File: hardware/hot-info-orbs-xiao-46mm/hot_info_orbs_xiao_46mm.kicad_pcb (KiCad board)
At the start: 2 copper layers, 224 x 52.8 mm, 13 parts, among them SW1 SW_Push, SW2 SW_Push, SW3 SW_Push, U2 XIAO ESP32-S3 Plus

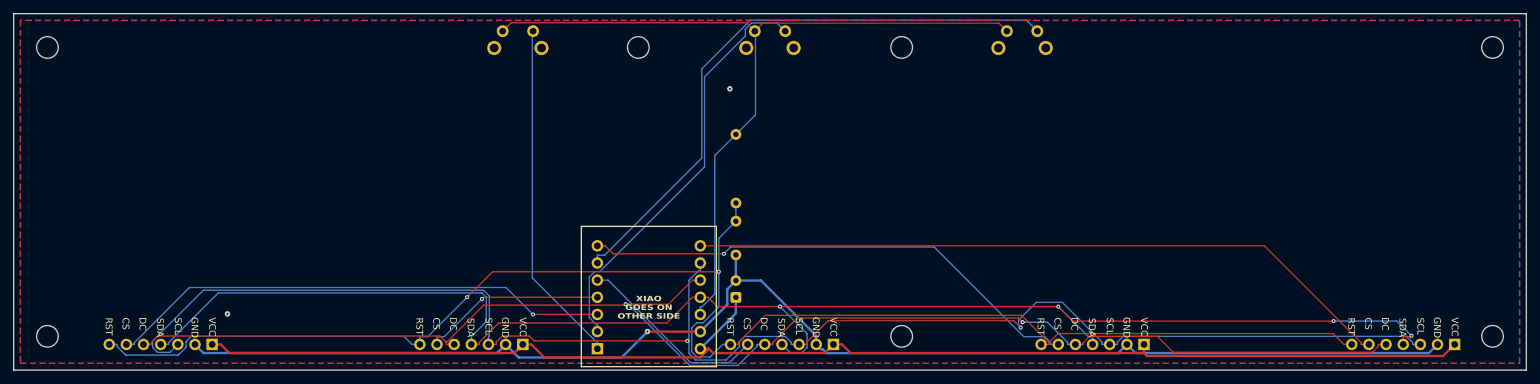
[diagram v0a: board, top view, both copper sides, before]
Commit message: board rev 2.4: Display circle on the front silk at each module position
Scott: "add circles indicating the display goes on that side, in the middle
put Display" and "increment the version". tools/display_marks.py puts a
O29.5 mm F.Silk circle with 2 mm "Display" at each DSn's 3D-model origin
(58.74 + n*46, y 81.0) and bumps rev 2.3 -> 2.4 (back silk, title block,
schematic rev). Copper, mask, outline and drill are run 3's; only the two
silk layers and the rev attribute changed.

Rejected the lit-area radius (16.25): at DS3 it crosses the front annular
rings of C1 pad 2 and XIAO pad 8, two "clipped by solder mask" DRC
warnings and two fab-cut gaps in the ring. 14.75 is the largest radius
that clears both. Rejected the module rim (19.05): past the board edge at
DS5. The DS3 circle crossing the XIAO box corner stays; silk over silk is
not a DRC item and the layout really is like that.

Package: fab/hot_info_orbs_xiao_46mm_2.4_run1_gerbers.zip; run 3 demoted
in fab/README.md. STEP regenerated and imported into overall assembly v8
(same transform, Position6), which also keeps the bezel/watch-crystal
occurrences that were sitting unsaved in the Fusion session.

Co-Authored-By: Claude Fable 5.1 <noreply@anthropic.com>
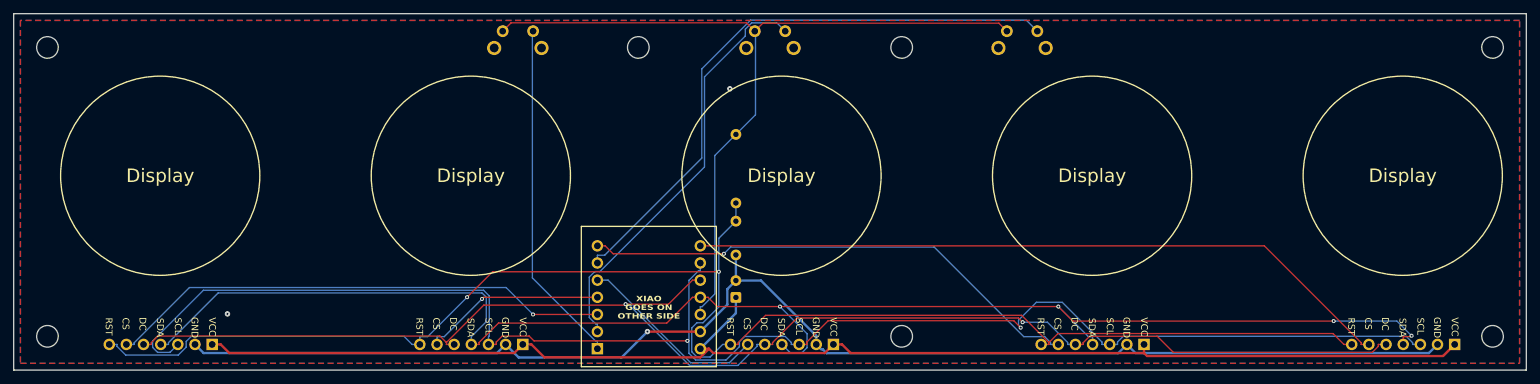
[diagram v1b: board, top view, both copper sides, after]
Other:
- board text added: "Display"
- board text added: "XIAO ESP32-S3 · rev 2.4 · 46 mm pitch"
- board text removed: "XIAO ESP32-S3 · rev 2.3 · 46 mm pitch"
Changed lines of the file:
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@@
 	(paper "A4")
 	(title_block
-		(rev "2.3")
+		(rev "2.4")
 	)
 	(layers
@@
 		)
 	)
+	(gr_circle
+		(center 58.74 81)
+		(end 73.49 81)
+		(stroke
+			(width 0.2)
+			(type default)
+		)
+		(fill no)
+		(layer "F.SilkS")
+	)
+	(gr_circle
+		(center 104.74 81)
+		(end 119.49 81)
+		(stroke
+			(width 0.2)
+			(type default)
+		)
+		(fill no)
+		(layer "F.SilkS")
+	)
 	(gr_rect
 		(start 121.1 88.5)
@@
 		(layer "F.SilkS")
 	)
+	(gr_circle
+		(center 150.739999 81)
+		(end 165.489999 81)
+		(stroke
+			(width 0.2)
+			(type default)
+		)
+		(fill no)
+		(layer "F.SilkS")
+	)
+	(gr_circle
+		(center 196.739999 81)
+		(end 211.489999 81)
+		(stroke
+			(width 0.2)
+			(type default)
+		)
+		(fill no)
+		(layer "F.SilkS")
+	)
+	(gr_circle
+		(center 242.739999 81)
+		(end 257.49 81)
+		(stroke
+			(width 0.2)
+			(type default)
+		)
+		(fill no)
+		(layer "F.SilkS")
+	)
 	(gr_line
 		(start 44.565137 83.469712)
@@
 		)
 	)
+	(gr_text "Display"
+		(at 58.74 81 0)
+		(layer "F.SilkS")
+		(effects
+			(font
+				(size 2 2)
+				(thickness 0.3)
+			)
+		)
+	)
+	(gr_text "Display"
+		(at 104.74 81 0)
+		(layer "F.SilkS")
+		(effects
+			(font
+				(size 2 2)
+				(thickness 0.3)
+			)
+		)
+	)
+	(gr_text "Display"
+		(at 150.739999 81 0)
+		(layer "F.SilkS")
+		(effects
+			(font
+				(size 2 2)
+				(thickness 0.3)
+			)
+		)
+	)
+	(gr_text "Display"
+		(at 196.739999 81 0)
+		(layer "F.SilkS")
+		(effects
+			(font
+				(size 2 2)
+				(thickness 0.3)
+			)
+		)
+	)
+	(gr_text "Display"
+		(at 242.739999 81 0)
+		(layer "F.SilkS")
+		(effects
+			(font
+				(size 2 2)
+				(thickness 0.3)
+			)
+		)
+	)
 	(gr_text "button\n"
 		(at 111.706633 64.63 0)
@@
 		)
 	)
-	(gr_text "XIAO ESP32-S3  ·  rev 2.3 · 46 mm pitch"
+	(gr_text "XIAO ESP32-S3  ·  rev 2.4 · 46 mm pitch"
 		(at 70.174 85.334052 0)
 		(layer "B.SilkS")
@@
 			(justify top mirror)
 		)
-		(render_cache "XIAO ESP32-S3  ·  rev 2.3 · 46 mm pitch" 0
+		(render_cache "XIAO ESP32-S3  ·  rev 2.4 · 46 mm pitch" 0
 			(polygon
 				(pts
@@
 			(polygon
 				(pts
-					(xy 62.649366 87.396578) (xy 62.784673 87.386522) (xy 62.907398 87.357291) (xy 63.019638 87.309505)
-					(xy 63.106201 87.252501) (xy 63.175326 87.186751) (xy 63.229006 87.111763) (xy 63.268277 87.026306)
-					(xy 63.276459 86.977945) (xy 63.266061 86.927416) (xy 63.234816 86.88611) (xy 63.189737 86.858592)
-					(xy 63.138462 86.849474) (xy 63.088583 86.861677) (xy 63.044184 86.90052) (xy 62.981292 86.995653)
-					(xy 62.924149 87.054398) (xy 62.84879 87.097136) (xy 62.760465 87.121853) (xy 62.649243 87.130841)
-					(xy 62.553323 87.120383) (xy 62.467125 87.089716) (xy 62.38827 87.038273) (xy 62.321098 86.966395)
-					(xy 62.282455 86.887521) (xy 62.269446 86.798549) (xy 62.279368 86.698783) (xy 62.307898 86.612508)
-					(xy 62.354636 86.536942) (xy 62.421121 86.470287) (xy 62.515519 86.410971) (xy 62.632332 86.3673)
-					(xy 62.776372 86.34096) (xy 62.849383 86.325314) (xy 62.894198 86.299377) (xy 62.919339 86.264663)
-					(xy 62.928047 86.218472) (xy 62.916674 86.1724) (xy 62.880512 86.132066) (xy 62.809223 86.095862)
-					(xy 62.482548 86.015506) (xy 62.397271 85.973759) (xy 62.340521 85.923549) (xy 62.304596 85.86027)
-					(xy 62.291306 85.782621) (xy 62.300583 85.707393) (xy 62.331016 85.644024) (xy 62.38424 85.589303)
-					(xy 62.454772 85.548921) (xy 62.546219 85.522633) (xy 62.664264 85.512977) (xy 62.755177 85.524172)
-					(xy 62.844638 85.558406) (xy 62.999121 85.655981) (xy 63.042977 85.678931) (xy 63.071539 85.684924)
-					(xy 63.121916 85.674527) (xy 63.165084 85.642792) (xy 63.19446 85.597339) (xy 63.204041 85.546804)
-					(xy 63.194349 85.500228) (xy 63.162461 85.451188) (xy 63.100154 85.397184) (xy 62.994969 85.337)
-					(xy 62.870474 85.28329) (xy 62.77254 85.255417) (xy 62.695772 85.247241) (xy 62.547793 85.256495)
-					(xy 62.423184 85.28244) (xy 62.318239 85.323069) (xy 62.229879 85.377422) (xy 62.149802 85.454052)
-					(xy 62.092972 85.544059) (xy 62.057845 85.650096) (xy 62.045475 85.776271) (xy 62.0572 85.903268)
-					(xy 62.089728 86.004857) (xy 62.141007 86.086352) (xy 62.211677 86.151315) (xy 62.304983 86.201131)
-					(xy 62.35835 86.220304) (xy 62.243847 86.274357) (xy 62.154529 86.340971) (xy 62.086508 86.420217)
-					(xy 62.037708 86.512832) (xy 62.007102 86.622319) (xy 61.99626 86.752509) (xy 62.008394 86.883214)
-					(xy 62.043817 87.001222) (xy 62.102471 87.109192) (xy 62.186159 87.208999) (xy 62.286846 87.291414)
-					(xy 62.396205 87.349397) (xy 62.516152 87.384522)
+					(xy 62.400652 85.214232) (xy 62.476948 85.255531) (xy 62.54544 85.328085) (xy 63.217719 86.31446)
+					(xy 63.3352 86.454655) (xy 63.394768 86.548185) (xy 63.410304 86.611215) (xy 63.398606 86.653118)
+					(xy 63.361536 86.685504) (xy 63.285985 86.70879) (xy 63.199227 86.716037) (xy 63.026354 86.719292)
+					(xy 62.423929 86.732237) (xy 62.422586 87.043158) (xy 62.425273 87.104707) (xy 62.427959 87.174561)
+					(xy 62.416595 87.270226) (xy 62.387911 87.328487) (xy 62.344879 87.361441) (xy 62.283123 87.37313)
+					(xy 62.226855 87.364527) (xy 62.190112 87.341581) (xy 62.16739 87.304042) (xy 62.158804 87.246002)
+					(xy 62.158804 86.740053) (xy 62.015236 86.740503) (xy 61.955227 86.733214) (xy 61.895989 86.706641)
+					(xy 61.863008 86.666346) (xy 61.851424 86.608528) (xy 61.864111 86.554409) (xy 61.902298 86.513907)
+					(xy 61.975498 86.48485) (xy 62.10275 86.472851) (xy 62.158804 86.474317) (xy 62.158804 86.466501)
+					(xy 62.423929 86.466501) (xy 62.993626 86.458685) (xy 62.771327 86.12759) (xy 62.423929 85.579411)
+					(xy 62.423929 86.466501) (xy 62.158804 86.466501) (xy 62.158804 85.33468) (xy 62.168699 85.275268)
+					(xy 62.195654 85.235478) (xy 62.241125 85.210119) (xy 62.313165 85.200346)
 				)
 			)

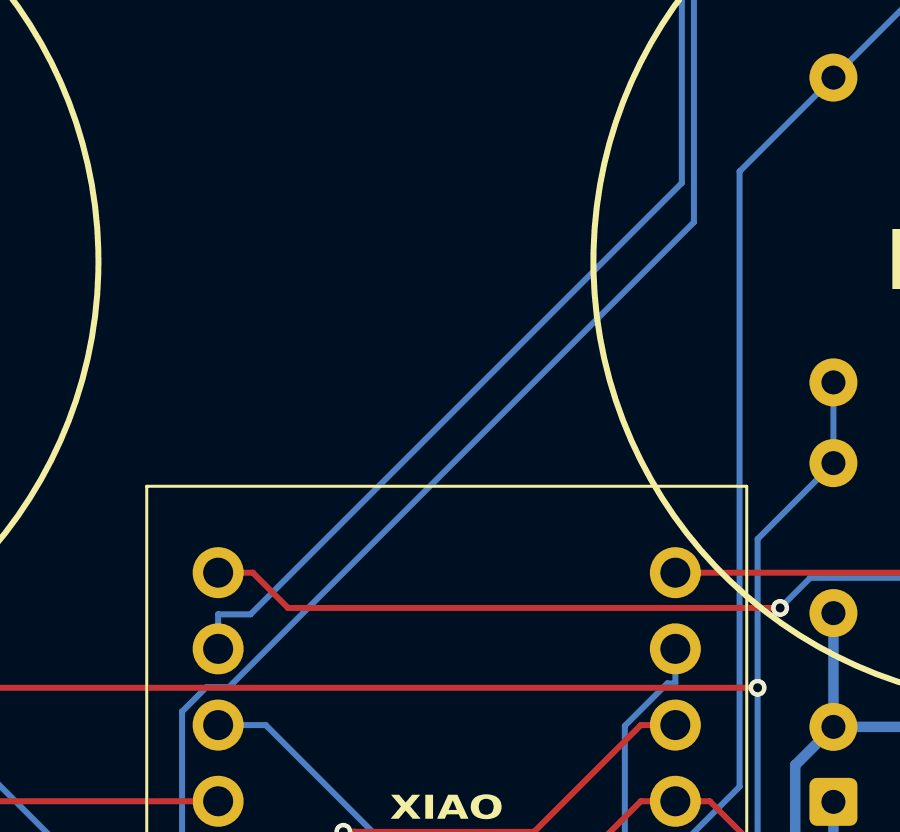
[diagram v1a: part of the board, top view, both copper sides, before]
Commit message: 46mm schematic: Scott's layout cleanup, title block to rev 2.4, one SW3 track straightened
Scott tidied the sheet on 2026-10-23. The edits sat uncommitted, so the package
sent to Yang that afternoon (built from 8dda9b9) still had the old layout:
U2 and the R1/C2 reset circuit sat apart from the rest and overlapped the title
block, which Yang read as "disconnected".

Connectivity is unchanged. XML netlists of 8dda9b9 and this commit have the
same 12 parts and the same 15 nets, pin for pin. ERC is 0. DRC shows the 3
known XIAO USB-C silk warnings, 0 unconnected, 0 parity. Board: one /SW3
dogleg near (123.5, 92.8) is now a direct run, and the pour was refilled.

Committed as Scott saved it, not re-laid out by script: the layout is his and
the netlist check is what shows it is safe.

Co-Authored-By: Claude Opus 5.5 <noreply@anthropic.com>
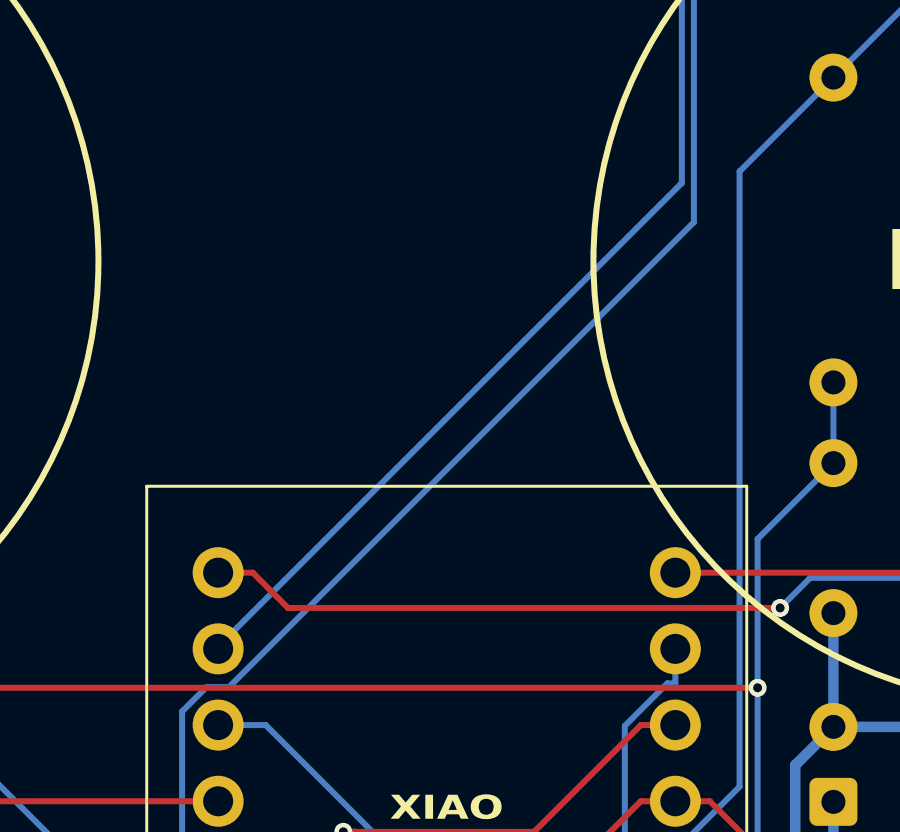
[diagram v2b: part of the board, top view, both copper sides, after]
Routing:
- net /SW3: track 89.1 -> 88.5 mm
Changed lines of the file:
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@@
 	)
 	(segment
-		(start 123.48 93.92)
-		(end 123.48 92.7683)
+		(start 138.9369 78.3911)
+		(end 123.48 93.848)
 		(width 0.2)
 		(layer "B.Cu")
@@
 	)
 	(segment
-		(start 138.9369 78.3911)
-		(end 124.5597 92.7683)
+		(start 123.48 93.848)
+		(end 123.48 93.92)
 		(width 0.2)
 		(layer "B.Cu")
@@
 	)
 	(segment
-		(start 124.5597 92.7683)
-		(end 123.48 92.7683)
+		(start 138.9369 65.176)
+		(end 138.9369 78.3911)
 		(width 0.2)
 		(layer "B.Cu")
@@
 		(width 0.2)
 		(layer "B.Cu")
-		(net "/SW3")
-	)
-	(segment
-		(start 138.9369 65.176)
-		(end 138.9369 78.3911)
-		(width 0.2)
-		(layer "B.Cu")

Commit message: 46 mm board rev 2.5: probe pads for 3V3, GND and 5V
Scott wanted test pads for debugging other people's builds. RST, SCLK,
MOSI, DC and CS1-CS5 were suggested; his call: "just add gnd 3.3v and 5v".

TP1 3V3 / TP2 GND / TP3 5V sit in one column at x 173.74, between the
DS3 and DS4 display circles, at 2.54 mm pitch so a 1x3 header or clip
fits. GND is in the middle so the black probe stays put. Pads are 2.0 mm
on a 1.00 mm drill, the socket drill already on the board, so no new
tool (T4 49 -> 52). Rail names and a box are on both silks. With the
modules fitted the pads stay clear, but the front labels end up under
DS4. The back labels are always readable.

Rejected:
- the gap beside DS3 at x ~153: the pads clipped DS3's front silk circle;
- a 1x8 row with the bus signals: Scott's call.

Footprint lib/_TestPoints.pretty is the stock TestPoint THT pad trimmed
to stack at 2.54 mm: courtyard r 1.25, no silk circle, reference on
F.Fab. Rejected editing the stock footprint in the board: it leaves three
lib_footprint_mismatch warnings for good.

The schematic has a TEST POINTS box beside POWER FLAGS, tops aligned at
y 160.02, wired the same way. The pads are in_bom no and the footprint
is exclude_from_bom: a bare hole needs nothing bought, and the BOM
export lists no TP.

The reroute (Freerouting, 0 unrouted, 0 violations) runs /MOSI round
C2 pad 2 on B.Cu, so that pad gets one back spoke instead of two. It
still has its own GND track and full front spokes. A one-pad .kicad_dru
rule (min_resolved_spokes 1) accepts that; aimed at pad 1 instead, the
error comes back. Rejected a DRC exclusion: the key format did not match
in three tries, and the next reroute would invalidate it anyway.

The reroute also dropped 2.4's three GND vias. Measured with island
removal off and on: the back pour now loses no island, so
stitch_islands.py was not rerun.

DRC 0 errors / 3 known U2 USB-C silk warnings / 0 unconnected / 0 parity.
ERC 0. New zip 2.5_run1; 2.4_run1 stays as uploaded for Scott'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
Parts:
- added TP1: 3V3, _TestPoints:TestPoint_THTPad_D2.0mm_Drill1.0mm_P2.54, F.Cu at (173.7, 78.5)
- added TP2: GND, _TestPoints:TestPoint_THTPad_D2.0mm_Drill1.0mm_P2.54, F.Cu at (173.7, 81.0)
- added TP3: 5V, _TestPoints:TestPoint_THTPad_D2.0mm_Drill1.0mm_P2.54, F.Cu at (173.7, 83.5)
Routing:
- net +5V: track 200.9 -> 229.0 mm
- net GND: track 202.5 -> 229.3 mm, vias 3 -> 0
- net /3V3: track 122.2 -> 139.6 mm
- net /MOSI: track 227.1 -> 209.7 mm, vias 4 -> 1
- net /SCLK: track 231.1 -> 217.9 mm, vias 2 -> 3
- net /RST: track 228.7 -> 237.6 mm
- net /CS1: track 75.0 -> 71.7 mm, vias 1 -> 0
- net /DC: track 212.5 -> 215.7 mm, vias 2 -> 4
- net /SW1: track 51.2 -> 54.1 mm
- net /CS3: track 28.4 -> 30.7 mm, vias 0 -> 1
- net /CS5: track 105.2 -> 107.3 mm, vias 0 -> 1
- net /SW2: track 62.3 -> 60.8 mm
- net /SW3: track 88.5 -> 89.6 mm
- net /CS4: track 75.3 -> 75.9 mm
- net /CS2: track 27.3 -> 26.8 mm, vias 1 -> 0
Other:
- board text added: "3V3"
- board text added: "5V"
- board text added: "GND"
- board text added: "XIAO ESP32-S3 · rev 2.5 · 46 mm pitch"
- board text removed: "XIAO ESP32-S3 · rev 2.4 · 46 mm pitch"

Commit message: Rev 2.5 run 2: "Test" beside the probe pads on both faces
Scott: add "Test" on the opposite side of the voltage labels, same side
of the board. tools/test_label.py puts it opposite the rail names on each
face: left of the column on the front, right of it (mirrored) on the back.

It is set vertically and centered on GND so one word labels all three
pads. Rejected horizontal text at the GND row: it would read as a fourth
row label beside GND only.

The change is silk only, so there was no reroute. The run 2 gerbers diff
against run 1 with only the timestamp lines differing on copper, mask,
outline and drill. DRC is unchanged: the 3 known silk-edge warnings,
0 unconnected, 0 parity. Run 1 is kept as the record, superseded before
it was sent.

Co-Authored-By: Claude Opus 5.5 <noreply@anthropic.com>
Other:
- board text added: "Test"
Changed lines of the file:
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@@
+		)
+	)
+	(gr_text "Test"
+		(at 171.44 81 90)
+		(layer "F.SilkS")
+		(effects
+			(font
+				(size 1 1)
+				(thickness 0.15)
+			)
 		)
 	)
@@
 		)
 	)
+	(gr_text "Test"
+		(at 176.04 81 90)
+		(layer "B.SilkS")
+		(effects
+			(font
+				(size 1 1)
+				(thickness 0.15)
+			)
+			(justify mirror)
+		)
+	)
